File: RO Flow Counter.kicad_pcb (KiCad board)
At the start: 2 copper layers, 100 x 55 mm, 72 parts, among them J1 LCD Power, J2 Conn_01x12, J3 Barrel_Jack, J5 Flow Meter, J6 Level Sensor (optional), J7 Conn_01x02, J8 Programming, K1 G5Q-1A, Q1 BC807, Q2 BC807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

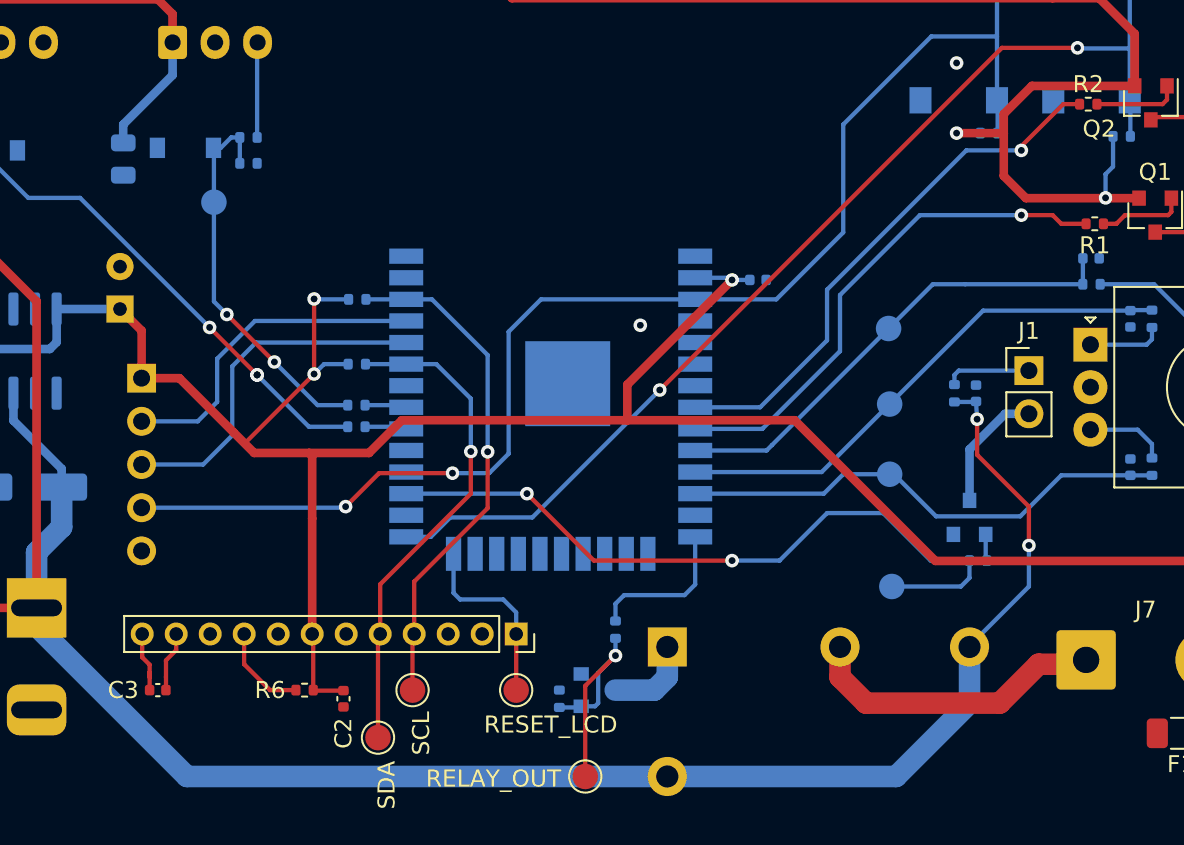
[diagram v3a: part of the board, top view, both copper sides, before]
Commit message: fix tracing, lcd pads
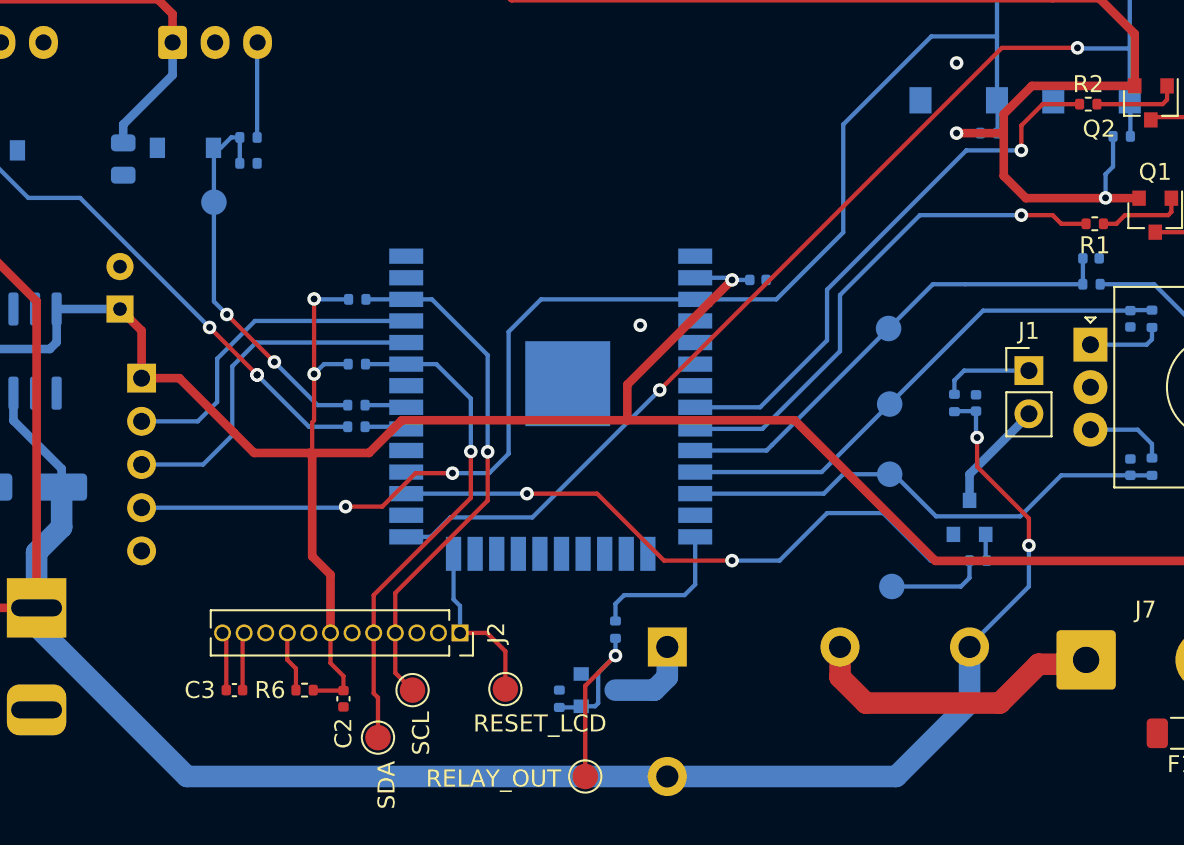
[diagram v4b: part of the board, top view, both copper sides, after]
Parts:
- J2: footprint Connector_PinSocket_2.00mm:PinSocket_1x12_P2.00mm_Vertical -> Connector_PinSocket_1.27mm:PinSocket_1x12_P1.27mm_Vertical
- moved C3 4.51 mm to (155.6, 100.8)
- moved J2 3.30 mm to (168.9, 97.5)
- moved TP8 0.64 mm to (171.6, 100.8)
- moved C1 0.57 mm to (199.3, 83.9)
- moved R5 0.57 mm to (198.0, 83.9)
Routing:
- net Net-(J2-Pad9): track 5.46 -> 3.58 mm
- net /display/RESET_DISPLAY: track 11.0 -> 10.1 mm
- net /display/SCL: track 30.1 -> 30.9 mm
- net Net-(J1-Pad2): track 7.81 -> 6.99 mm
- net /mcu/ERROR_OUT: track 32.1 -> 32.9 mm
- net +24V: track 164.9 -> 164.3 mm
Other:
- board text added: "3V3"
- board text added: "GND"
- board text added: "RO Flow counter v0.2"
- board text added: "Reset"
- board text removed: "RO Flow counter v0.1"

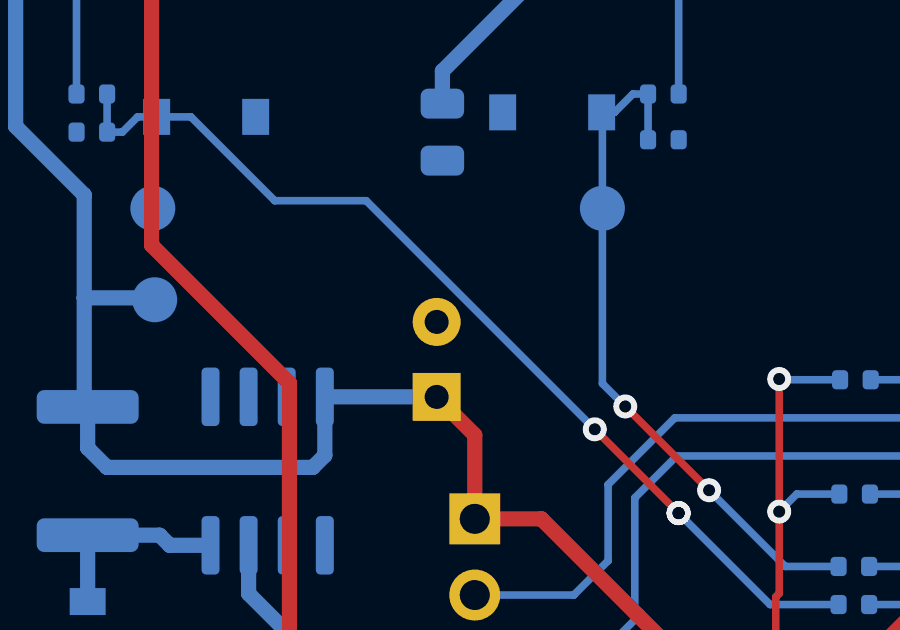
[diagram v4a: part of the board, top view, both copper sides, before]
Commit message: fix voltage level on flow sensor
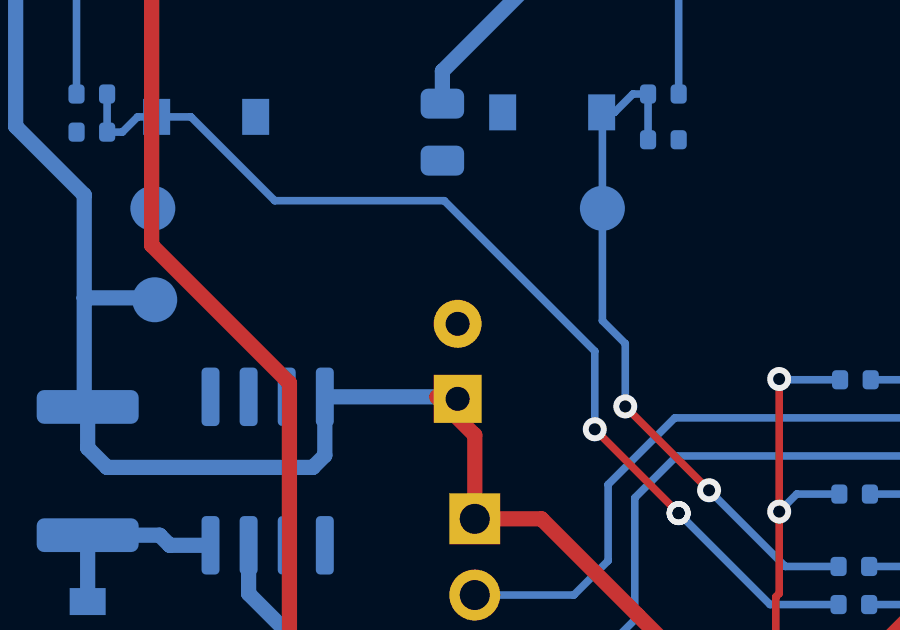
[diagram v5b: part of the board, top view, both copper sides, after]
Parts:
- R15: value 42.2k -> 5k6
- R19: value 5k6 -> 10k
- moved C6 0.70 mm to (149.6, 78.5)
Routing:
- net Net-(D5-Pad1): track 35.7 -> 37.2 mm

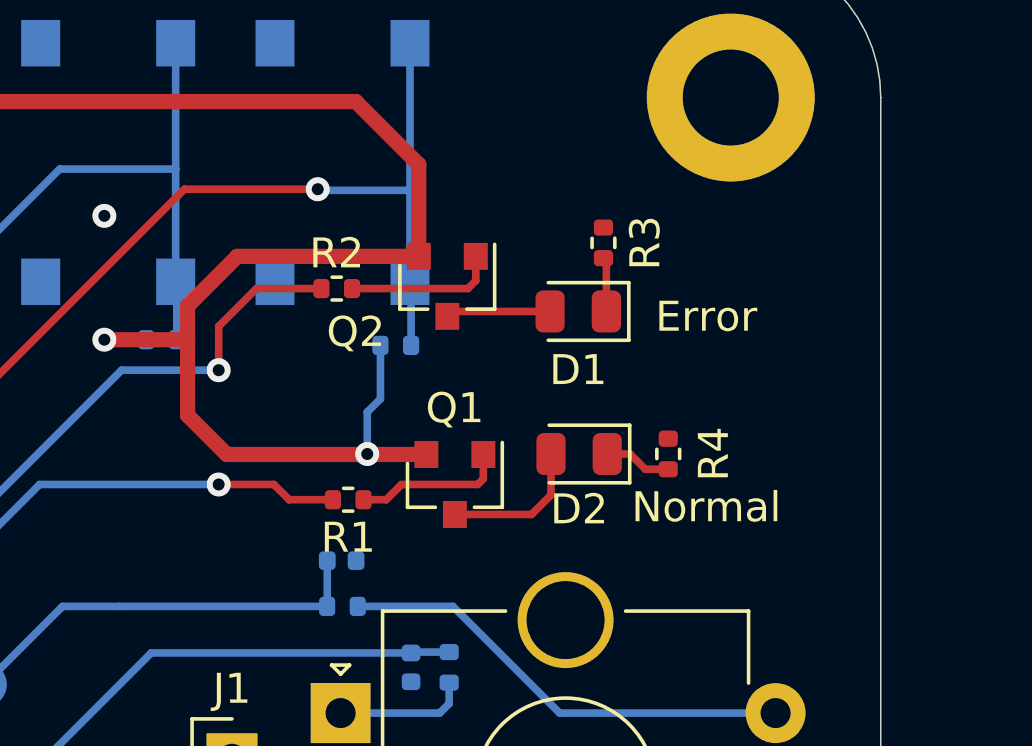
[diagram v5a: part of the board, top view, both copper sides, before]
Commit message: use mosfet for led instead of bjt
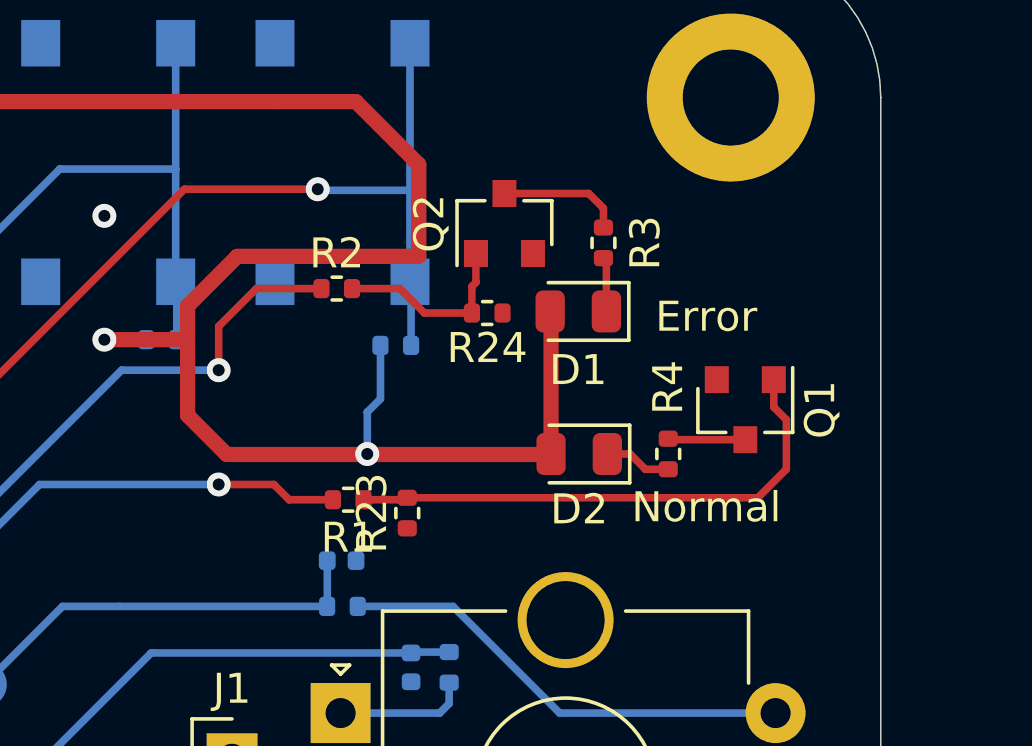
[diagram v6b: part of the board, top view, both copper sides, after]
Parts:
- added R23: 10k, Resistor_SMD:R_0402_1005Metric, F.Cu at (208.2, 73.9)
- added R24: 10k, Resistor_SMD:R_0402_1005Metric, F.Cu at (210.9, 67.2)
- Q1, Q2: value BC807 -> 2N7002E
- R1, R2: value 10k -> 1k
- moved Q1 10.00 mm to (219.5, 70.4)
- moved Q2 2.83 mm to (211.5, 64.2), turned to 90 degrees
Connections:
- D1 pad 2: Net-(D1-Pad2) -> +3V3
- D2 pad 2: Net-(D2-Pad2) -> +3V3
- Q1 pad 2: +3V3 -> GND
- Q1 pad 3: Net-(D2-Pad2) -> Net-(Q1-Pad3)
- Q2 pad 2: +3V3 -> GND
- Q2 pad 3: Net-(D1-Pad2) -> Net-(Q2-Pad3)
- R3 pad 2: GND -> Net-(Q2-Pad3)
- R4 pad 2: GND -> Net-(Q1-Pad3)
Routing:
- net Net-(Q1-Pad1): track 5.10 -> 17.7 mm
- net +3V3: track 274.1 -> 283.0 mm
- net Net-(D2-Pad2): track 4.84 -> 0.00 mm
- net Net-(Q2-Pad3): track 0.00 -> 4.15 mm
- net Net-(D1-Pad2): track 3.47 -> 0.00 mm
- net Net-(Q1-Pad3): track 0.00 -> 2.58 mm
- net Net-(Q2-Pad1): track 5.04 -> 6.37 mm

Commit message: finish v2
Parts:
- added D6: WiFi, LED_SMD:LED_0805_2012Metric, F.Cu at (213.6, 62.0)
- added Q5: 2N7002E, Package_TO_SOT_SMD:SOT-23, F.Cu at (209.8, 61.2)
- added R25: 154, Resistor_SMD:R_0402_1005Metric, F.Cu at (210.6, 63.6)
- added R26: 1k, Resistor_SMD:R_0402_1005Metric, F.Cu at (205.7, 61.5)
- added R27: 10k, Resistor_SMD:R_0402_1005Metric, F.Cu at (207.3, 62.0)
- C1: value 100nF -> 22uF; footprint Capacitor_SMD:C_0402_1005Metric -> Capacitor_SMD:C_0805_2012Metric
- J7: footprint Connector_Wire:SolderWire-0.75sqmm_1x02_P7mm_D1.25mm_OD3.5mm -> Connector_Wire:SolderWire-2.5sqmm_1x02_P8.8mm_D2.4mm_OD4.4mm
- moved Q1 9.74 mm to (209.8, 71.3)
- moved R4 6.69 mm to (210.5, 73.8), turned to 180 degrees
- moved R3 5.75 mm to (210.5, 68.7), turned to 180 degrees
- moved R24 3.55 mm to (207.3, 66.9), turned to 90 degrees
- moved Q2 2.62 mm to (209.8, 66.2), turned to 270 degrees
- moved R23 2.05 mm to (207.3, 72.0)
- moved R1 1.91 mm to (205.7, 71.6)
- moved C1 1.86 mm to (197.5, 83.3)
- moved F1 1.78 mm to (211.4, 105.2)
- moved R5 1.24 mm to (199.2, 83.9)
- moved J7 0.58 mm to (205.2, 99.1)
- moved D1 0.36 mm to (213.6, 67.1), turned to 0 degrees
- moved D2 0.36 mm to (213.6, 71.9), turned to 0 degrees
- moved R2 0.19 mm to (205.7, 66.4)
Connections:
- U2 pad 16: (no net) -> /mcu/LED_WIFI
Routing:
- net /mcu/LED_WIFI: track 0.00 -> 44.7 mm, vias 0 -> 1
- net Net-(Q1-Pad1): track 17.7 -> 5.50 mm
- net Net-(Q5-Pad1): track 0.00 -> 5.60 mm
- net Net-(D6-Pad1): track 0.00 -> 2.85 mm
- net Net-(Q2-Pad3): track 4.15 -> 1.64 mm
- net /display/BACKLIGHT_LCD: track 42.9 -> 40.6 mm
- net Net-(F1-Pad1): track 4.32 -> 6.56 mm
- net /mcu/NORMAL_OPERATION_OUT: track 30.3 -> 28.2 mm
- net Net-(Q5-Pad3): track 0.00 -> 1.59 mm
- net Net-(J1-Pad1): track 5.44 -> 4.27 mm
- net /mcu/ERROR_OUT: track 32.9 -> 31.7 mm
- net Net-(D1-Pad1): track 1.82 -> 2.90 mm
- net /mcu/RE_A: track 30.8 -> 31.8 mm
- net Net-(Q1-Pad3): track 2.58 -> 1.63 mm
- net Net-(D2-Pad1): track 2.24 -> 3.18 mm
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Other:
- board text added: "WiFi"

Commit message: fix ro GND pad
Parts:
- added G***: LOGO, Custom Footprints:puppy_symbol, B.Cu at (177.0, 64.0)
- R25: value 154 -> 10
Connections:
- SW2 pad S1: +3V3 -> GND
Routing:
- net +3V3: track 283.9 -> 227.7 mm
